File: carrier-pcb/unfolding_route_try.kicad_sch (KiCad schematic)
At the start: 66 parts, among them J1 USB_C_Receptacle_USB2.0, J2 Conn_01x04_Female, J3 1-338068-8, U1 TCA9548APWR, U10 DRV2605LDGS, U11 DRV2605LDGS, U12 BMX160, U2 TCA9548APWR, U3 DRV2605LDGS, U4 DRV2605LDGS, U5 DRV2605LDGS, U6 DRV2605LDGS, U7 DRV2605LDGS, U8 DRV2605LDGS, U9 DRV2605LDGS

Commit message: New routing
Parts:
- removed J2: Conn_01x04_Female, Connector_Wire:SolderWire-0.1sqmm_1x04_P3.6mm_D0.4mm_OD1mm, symbol Connector:Conn_01x04_Female
- added J2, J4, J5, J6: Conn_01x01_Female, Connector_Wire:SolderWirePad_1x01_SMD_1x2mm, symbol Connector:Conn_01x01_Female
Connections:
- net +5V: now also J2.1 (Pin_1)
- net GND: now also J6.1 (Pin_1)
- net USB_D+: now also J4.1 (Pin_1)
- net USB_D-: now also J5.1 (Pin_1)
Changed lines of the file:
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@@
     (stroke (width 0) (type solid) (color 0 0 0 0))
   )
-  (wire (pts (xy 38.1 99.06) (xy 43.18 99.06))
+  (wire (pts (xy 35.56 99.06) (xy 43.18 99.06))
     (stroke (width 0) (type solid) (color 0 0 0 0))
   )
-  (wire (pts (xy 38.1 101.6) (xy 48.26 101.6))
+  (wire (pts (xy 35.56 101.6) (xy 48.26 101.6))
     (stroke (width 0) (type solid) (color 0 0 0 0))
   )
-  (wire (pts (xy 38.1 104.14) (xy 48.26 104.14))
+  (wire (pts (xy 35.56 104.14) (xy 48.26 104.14))
     (stroke (width 0) (type solid) (color 0 0 0 0))
   )
-  (wire (pts (xy 38.1 106.68) (xy 43.18 106.68))
+  (wire (pts (xy 35.56 106.68) (xy 43.18 106.68))
     (stroke (width 0) (type solid) (color 0 0 0 0))
   )
@@
     (pin "1")
   )
+  (symbol (lib_id "Connector:Conn_01x01_Female") (at 30.48 99.06 180) (unit 1)
+    (in_bom yes) (on_board yes) (fields_autoplaced)
+    (property "Reference" "J2" (id 0) (at 33.1724 95.25 0))
+    (property "Value" "Conn_01x01_Female" (id 1) (at 33.1724 97.79 0))
+    (property "Footprint" "Connector_Wire:SolderWirePad_1x01_SMD_1x2mm" (id 2) (at 30.48 99.06 0)
+      (effects (font (size 1.27 1.27)) hide)
+    )
+    (property "Datasheet" "~" (id 3) (at 30.48 99.06 0)
+      (effects (font (size 1.27 1.27)) hide)
+    )
+    (pin "1")
+  )
+  (symbol (lib_id "Connector:Conn_01x01_Female") (at 30.48 101.6 180) (unit 1)
+    (in_bom yes) (on_board yes) (fields_autoplaced)
+    (property "Reference" "J4" (id 0) (at 33.1724 97.79 0))
+    (property "Value" "Conn_01x01_Female" (id 1) (at 33.1724 100.33 0))
+    (property "Footprint" "Connector_Wire:SolderWirePad_1x01_SMD_1x2mm" (id 2) (at 30.48 101.6 0)
+      (effects (font (size 1.27 1.27)) hide)
+    )
+    (property "Datasheet" "~" (id 3) (at 30.48 101.6 0)
+      (effects (font (size 1.27 1.27)) hide)
+    )
+    (pin "1")
+  )
+  (symbol (lib_id "Connector:Conn_01x01_Female") (at 30.48 104.14 180) (unit 1)
+    (in_bom yes) (on_board yes) (fields_autoplaced)
+    (property "Reference" "J5" (id 0) (at 33.1724 100.33 0))
+    (property "Value" "Conn_01x01_Female" (id 1) (at 33.1724 102.87 0))
+    (property "Footprint" "Connector_Wire:SolderWirePad_1x01_SMD_1x2mm" (id 2) (at 30.48 104.14 0)
+      (effects (font (size 1.27 1.27)) hide)
+    )
+    (property "Datasheet" "~" (id 3) (at 30.48 104.14 0)
+      (effects (font (size 1.27 1.27)) hide)
+    )
+    (pin "1")
+  )
+  (symbol (lib_id "Connector:Conn_01x01_Female") (at 30.48 106.68 180) (unit 1)
+    (in_bom yes) (on_board yes) (fields_autoplaced)
+    (property "Reference" "J6" (id 0) (at 33.1724 102.87 0))
+    (property "Value" "Conn_01x01_Female" (id 1) (at 33.1724 105.41 0))
+    (property "Footprint" "Connector_Wire:SolderWirePad_1x01_SMD_1x2mm" (id 2) (at 30.48 106.68 0)
+      (effects (font (size 1.27 1.27)) hide)
+    )
+    (property "Datasheet" "~" (id 3) (at 30.48 106.68 0)
+      (effects (font (size 1.27 1.27)) hide)
+    )
+    (pin "1")
+  )
   (symbol (lib_id "power:GND") (at 30.48 266.7 0) (unit 1)
     (in_bom yes) (on_board yes)
@@
     (pin "2")
   )
-  (symbol (lib_id "Connector:Conn_01x04_Female") (at 33.02 104.14 180) (unit 1)
-    (in_bom yes) (on_board yes) (fields_autoplaced)
-    (property "Reference" "J2" (id 0) (at 35.7124 95.25 0))
-    (property "Value" "Conn_01x04_Female" (id 1) (at 35.7124 97.79 0))
-    (property "Footprint" "Connector_Wire:SolderWire-0.1sqmm_1x04_P3.6mm_D0.4mm_OD1mm" (id 2) (at 33.02 104.14 0)
-      (effects (font (size 1.27 1.27)) hide)
-    )
-    (property "Datasheet" "~" (id 3) (at 33.02 104.14 0)
-      (effects (font (size 1.27 1.27)) hide)
-    )
-    (pin "1")
-    (pin "2")
-    (pin "3")
-    (pin "4")
-  )
   (symbol (lib_id "pspice:DIODE") (at 74.93 50.8 90) (unit 1)
     (in_bom yes) (on_board yes) (fields_autoplaced)
@@
       (reference "J1") (unit 1) (value "USB_C_Receptacle_USB2.0") (footprint "Connector_USB:USB_C_Receptacle_HRO_TYPE-C-31-M-12")
     )
-    (path "/a6b2795c-5490-47a0-885f-80e194c7f0a5"
-      (reference "J2") (unit 1) (value "Conn_01x04_Female") (footprint "Connector_Wire:SolderWire-0.1sqmm_1x04_P3.6mm_D0.4mm_OD1mm")
+    (path "/ac49e00a-5ed5-4857-8006-1aed13ae61c1"
+      (reference "J2") (unit 1) (value "Conn_01x01_Female") (footprint "Connector_Wire:SolderWirePad_1x01_SMD_1x2mm")
     )
     (path "/5cf17887-f1ff-4a1a-8009-890a9f14e0e0"
       (reference "J3") (unit 1) (value "1-338068-8") (footprint "footprints:1-338068-8")
     )
+    (path "/4d8a46ed-41fd-4cd4-b602-075741d0d23f"
+      (reference "J4") (unit 1) (value "Conn_01x01_Female") (footprint "Connector_Wire:SolderWirePad_1x01_SMD_1x2mm")
+    )
+    (path "/b3db4dfd-ded3-43ed-88e3-9230a4007ffc"
+      (reference "J5") (unit 1) (value "Conn_01x01_Female") (footprint "Connector_Wire:SolderWirePad_1x01_SMD_1x2mm")
+    )
+    (path "/60bd3e5d-30af-4910-bdbe-ab68030b2837"
+      (reference "J6") (unit 1) (value "Conn_01x01_Female") (footprint "Connector_Wire:SolderWirePad_1x01_SMD_1x2mm")
+    )
     (path "/223c5957-c5cf-487a-a2a3-5023ac54cb65"

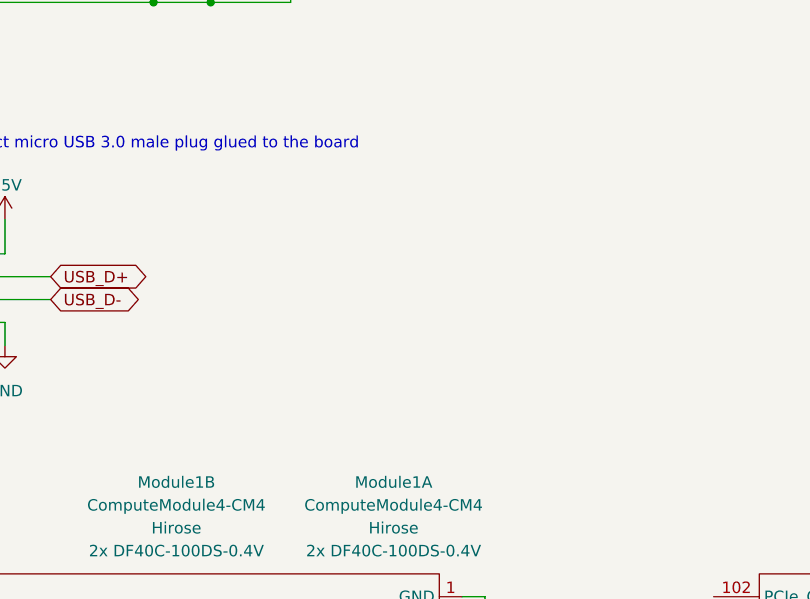
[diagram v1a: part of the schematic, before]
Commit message: finish new routing with diff pair. export stp file.
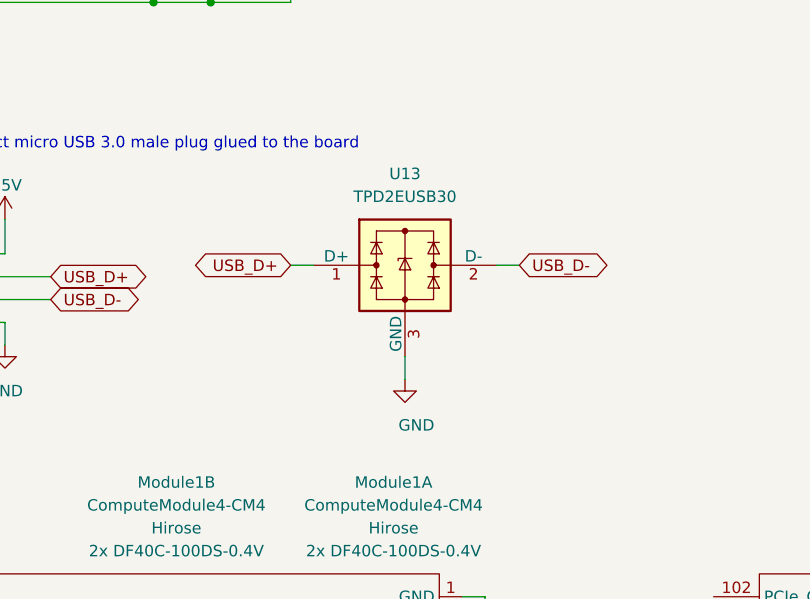
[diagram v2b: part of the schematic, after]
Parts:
- added U13: TPD2EUSB30, Package_TO_SOT_SMD:Texas_DRT-3, symbol Power_Protection:TPD2EUSB30
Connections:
- net GND: now also U13.3 (GND)
- net USB_D+: now also U13.1 (D+)
- net USB_D-: now also U13.2 (D-)
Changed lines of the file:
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@@
     (stroke (width 0) (type solid) (color 0 0 0 0))
   )
+  (wire (pts (xy 74.93 100.33) (xy 77.47 100.33))
+    (stroke (width 0) (type solid) (color 0 0 0 0))
+  )
+  (wire (pts (xy 87.63 110.49) (xy 87.63 113.03))
+    (stroke (width 0) (type solid) (color 0 0 0 0))
+  )
   (wire (pts (xy 93.98 137.16) (xy 96.52 137.16))
     (stroke (width 0) (type solid) (color 0 0 0 0))
@@
     (stroke (width 0) (type solid) (color 0 0 0 0))
   )
+  (wire (pts (xy 97.79 100.33) (xy 100.33 100.33))
+    (stroke (width 0) (type solid) (color 0 0 0 0))
+  )
   (wire (pts (xy 101.6 231.14) (xy 101.6 233.68))
     (stroke (width 0) (type solid) (color 0 0 0 0))
@@
     )
   )
+  (global_label "USB_D+" (shape bidirectional) (at 74.93 100.33 180)
+    (effects (font (size 1.27 1.27)) (justify right))
+    (property "Intersheet References" "${INTERSHEET_REFS}" (id 0) (at 64.8969 100.4094 0)
+      (effects (font (size 1.27 1.27)) (justify right) hide)
+    )
+  )
   (global_label "RX" (shape input) (at 99.06 200.66 0)
     (effects (font (size 1.27 1.27)) (justify left))
@@
     )
   )
+  (global_label "USB_D-" (shape bidirectional) (at 100.33 100.33 0)
+    (effects (font (size 1.27 1.27)) (justify left))
+    (property "Intersheet References" "${INTERSHEET_REFS}" (id 0) (at 110.3631 100.2506 0)
+      (effects (font (size 1.27 1.27)) (justify left) hide)
+    )
+  )
   (global_label "SCL_bmx160" (shape input) (at 149.86 71.12 180)
     (effects (font (size 1.27 1.27)) (justify right))
@@
     (pin "1")
   )
+  (symbol (lib_id "power:GND") (at 87.63 113.03 0) (unit 1)
+    (in_bom yes) (on_board yes)
+    (property "Reference" "#PWR0108" (id 0) (at 87.63 119.38 0)
+      (effects (font (size 1.27 1.27)) hide)
+    )
+    (property "Value" "GND" (id 1) (at 88.9 118.11 0))
+    (property "Footprint" "" (id 2) (at 87.63 113.03 0)
+      (effects (font (size 1.27 1.27)) hide)
+    )
+    (property "Datasheet" "" (id 3) (at 87.63 113.03 0)
+      (effects (font (size 1.27 1.27)) hide)
+    )
+    (pin "1")
+  )
   (symbol (lib_id "power:GND") (at 96.52 265.43 0) (unit 1)
     (in_bom yes) (on_board yes)
@@
     (pin "2")
   )
+  (symbol (lib_id "Power_Protection:TPD2EUSB30") (at 87.63 100.33 0) (unit 1)
+    (in_bom yes) (on_board yes)
+    (property "Reference" "U13" (id 0) (at 87.63 90.17 0))
+    (property "Value" "TPD2EUSB30" (id 1) (at 87.63 92.71 0))
+    (property "Footprint" "Package_TO_SOT_SMD:Texas_DRT-3" (id 2) (at 68.58 107.95 0)
+      (effects (font (size 1.27 1.27)) hide)
+    )
+    (property "Datasheet" "http://www.ti.com/lit/ds/symlink/tpd2eusb30a.pdf" (id 3) (at 87.63 100.33 0)
+      (effects (font (size 1.27 1.27)) hide)
+    )
+    (property "Manufacturer" "Texas Instruments" (id 4) (at 87.63 100.33 0)
+      (effects (font (size 1.27 1.27)) hide)
+    )
+    (property "MPN" "TPD2EUSB30DRTR" (id 5) (at 87.63 100.33 0)
+      (effects (font (size 1.27 1.27)) hide)
+    )
+    (property "Digi-Key_PN" "296-25509-1-ND" (id 6) (at 87.63 100.33 0)
+      (effects (font (size 1.27 1.27)) hide)
+    )
+    (pin "1")
+    (pin "2")
+    (pin "3")
+  )
   (symbol (lib_id "Driver_Haptic:DRV2605LDGS") (at 308.61 38.1 0) (unit 1)
     (in_bom yes) (on_board yes)
@@
       (reference "#PWR0107") (unit 1) (value "GND") (footprint "")
     )
+    (path "/2612e7f5-e996-49ce-a33c-9473e9d5a784"
+      (reference "#PWR0108") (unit 1) (value "GND") (footprint "")
+    )
     (path "/91de5f95-5f20-4935-b831-c26bba9c0447"
       (reference "C1") (unit 1) (value "1u") (footprint "Capacitor_SMD:C_0603_1608Metric")
@@
       (reference "U12") (unit 1) (value "BMX160") (footprint "BMX160:PQFN50P250X300X100-14N")
     )
+    (path "/96afad6f-495f-4e72-bbfb-b283a69faa97"
+      (reference "U13") (unit 1) (value "TPD2EUSB30") (footprint "Package_TO_SOT_SMD:Texas_DRT-3")
+    )
   )

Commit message: change diode footprint
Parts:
- C1: footprint Capacitor_SMD:C_0603_1608Metric -> Diode_SMD:D_SMA-SMB_Universal_Handsoldering
- D1: footprint Diode_SMD:D_0603_1608Metric -> Diode_SMD:D_SMA
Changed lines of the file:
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@@
       (effects (font (size 1.27 1.27)) (justify left))
     )
-    (property "Footprint" "Capacitor_SMD:C_0603_1608Metric" (id 2) (at 233.68 57.15 0)
+    (property "Footprint" "Diode_SMD:D_SMA-SMB_Universal_Handsoldering" (id 2) (at 233.68 57.15 0)
       (effects (font (size 1.27 1.27)) hide)
     )
@@
       (effects (font (size 1.27 1.27)) (justify right))
     )
-    (property "Footprint" "Diode_SMD:D_0603_1608Metric" (id 2) (at 74.93 50.8 0)
+    (property "Footprint" "Diode_SMD:D_SMA" (id 2) (at 74.93 50.8 0)
       (effects (font (size 1.27 1.27)) hide)
     )
@@
     )
     (path "/91de5f95-5f20-4935-b831-c26bba9c0447"
-      (reference "C1") (unit 1) (value "1u") (footprint "Capacitor_SMD:C_0603_1608Metric")
+      (reference "C1") (unit 1) (value "1u") (footprint "Diode_SMD:D_SMA-SMB_Universal_Handsoldering")
     )
     (path "/36b91946-7ae6-4527-b4db-b08ffcb31f9c"
@@
     )
     (path "/e8d31ee4-38f5-4ce1-ab90-c542bfff504f"
-      (reference "D1") (unit 1) (value "RND SMBJ5A") (footprint "Diode_SMD:D_0603_1608Metric")
+      (reference "D1") (unit 1) (value "RND SMBJ5A") (footprint "Diode_SMD:D_SMA")
     )
     (path "/b7f76a32-8469-43c8-9201-e25021d1cfb0"

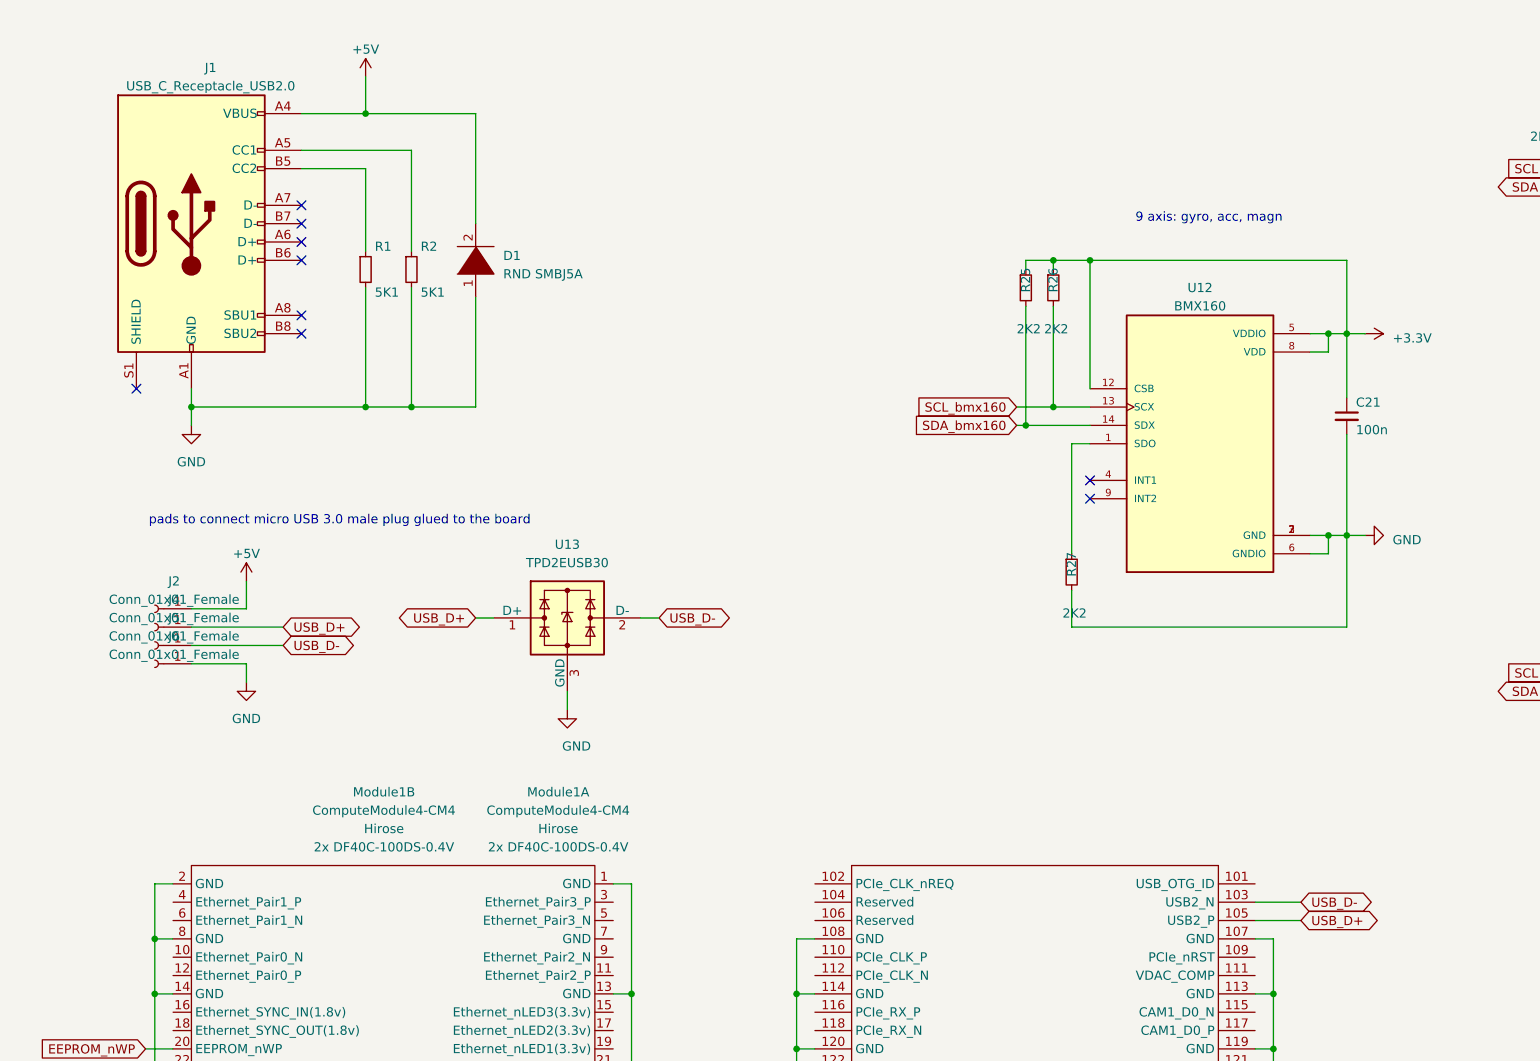
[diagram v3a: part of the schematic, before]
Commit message: change ESD protection. change usb plug. reroute
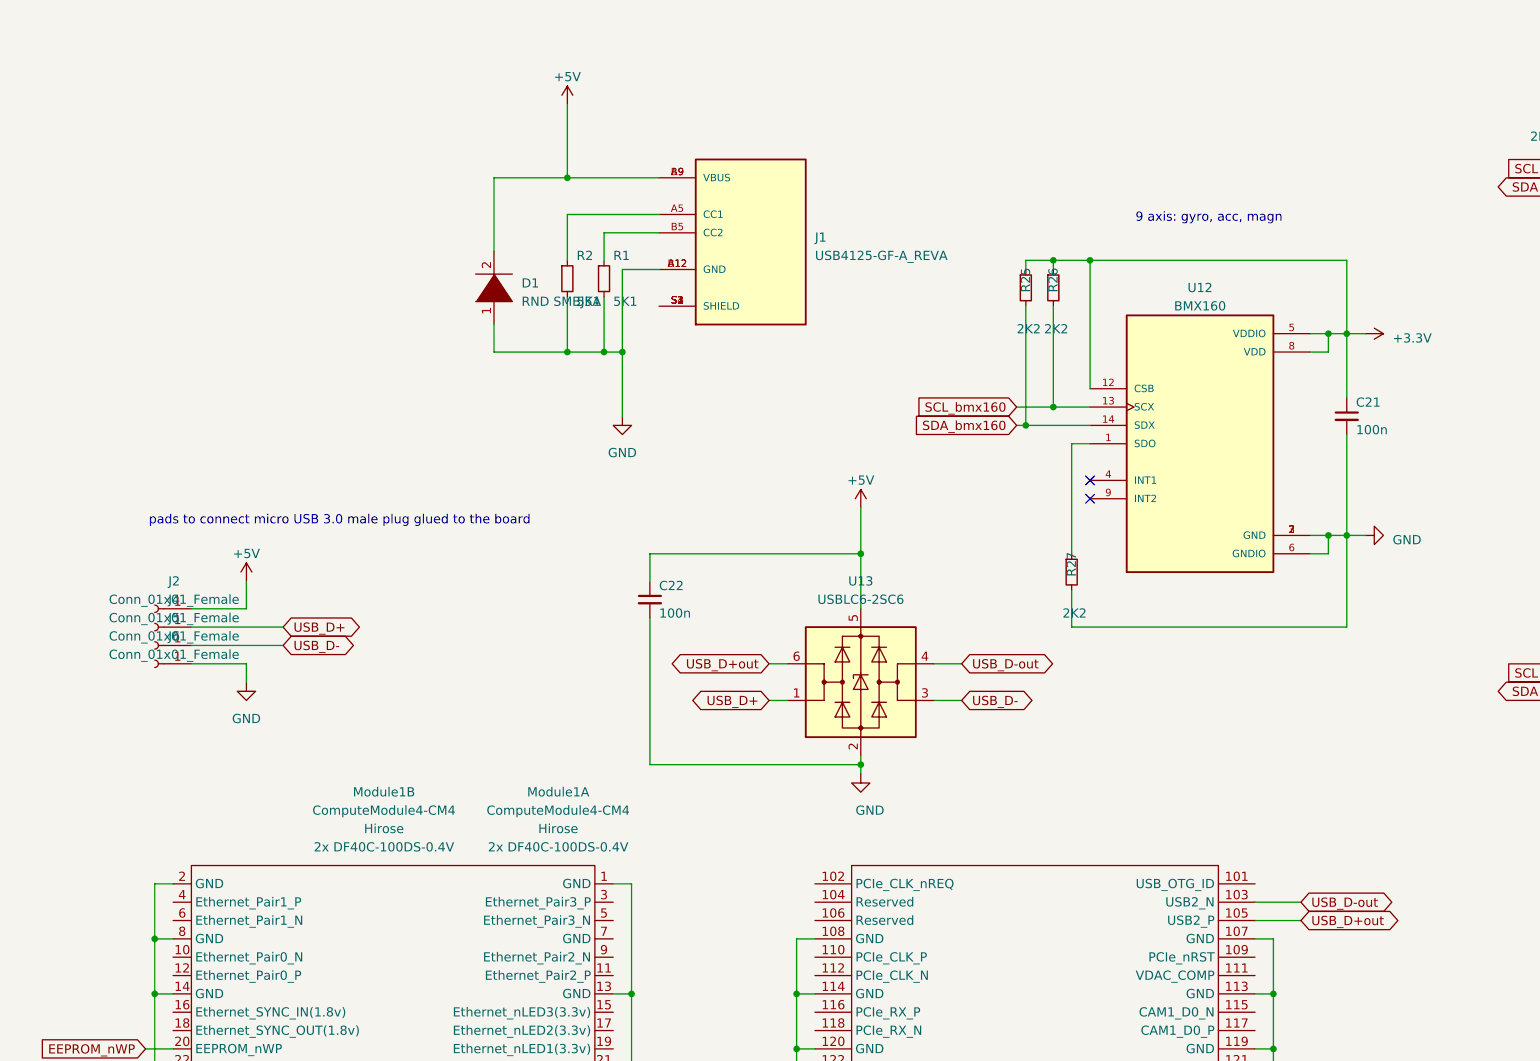
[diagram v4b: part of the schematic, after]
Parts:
- removed J1: USB_C_Receptacle_USB2.0, Connector_USB:USB_C_Receptacle_HRO_TYPE-C-31-M-12, symbol Connector:USB_C_Receptacle_USB2.0
- removed U13: TPD2EUSB30, Package_TO_SOT_SMD:Texas_DRT-3, symbol Power_Protection:TPD2EUSB30
- added C22: 100n, Capacitor_SMD:C_0603_1608Metric, symbol Device:C_Small
- added J1: USB4125-GF-A_REVA, USB4125-GF-A_REVA:GCT_USB4125-GF-A_REVA, symbol USB4125-GF-A_REVA:USB4125-GF-A_REVA
- added U13: USBLC6-2SC6, Package_TO_SOT_SMD:SOT-23-6, symbol Power_Protection:USBLC6-2SC6
- C1: footprint Diode_SMD:D_SMA-SMB_Universal_Handsoldering -> own:CUI_UJC-HP-3-SMT-TR
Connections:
- net +5V: now also C22.1, J1.A9 (VBUS), J1.B9 (VBUS), U13.5 (VBUS)
- net GND: now also C22.2, J1.A12 (GND), J1.B12 (GND), U13.2 (GND)
- net USB_D+: now also U13.1 (I/O1); no longer Module1.105 (USB2_P)
- net USB_D-: now also U13.3 (I/O2); no longer Module1.103 (USB2_N)
- net at R2.1: now also J1.A5 (CC1)
- net at R1.1: now also J1.B5 (CC2)
- new net: J1.S1 (SHIELD), J1.S2 (SHIELD), J1.S3 (SHIELD), J1.S4 (SHIELD)
- new net USB_D+out: Module1.105 (USB2_P), U13.6 (I/O1)
- new net USB_D-out: Module1.103 (USB2_N), U13.4 (I/O2)
- no-connect marks 23 -> 16
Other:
- moved on the sheet: R1, R2
